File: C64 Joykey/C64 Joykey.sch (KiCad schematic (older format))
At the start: 25 parts, among them J1 Port_1, J2 Port_2, M1 Mounting, M2 Mounting, M3 Mounting, M4 Mounting, SW1 FIRE1, SW2 FIRE2, SW3 FIRE3, SW4 UP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

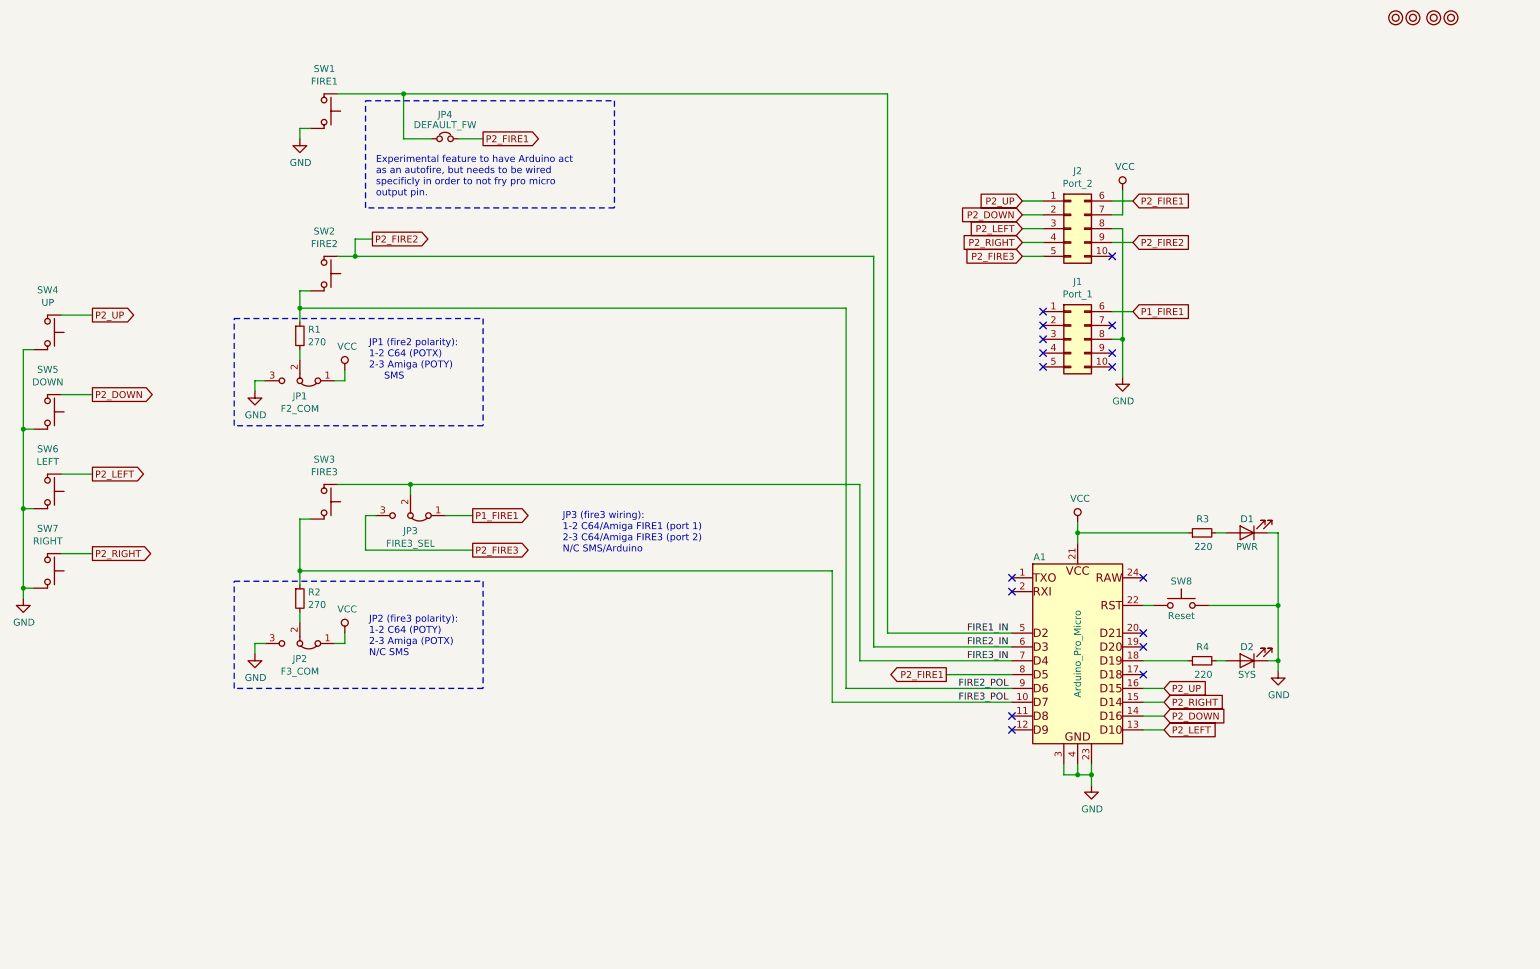
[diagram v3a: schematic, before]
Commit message: Tweaked PCB layout
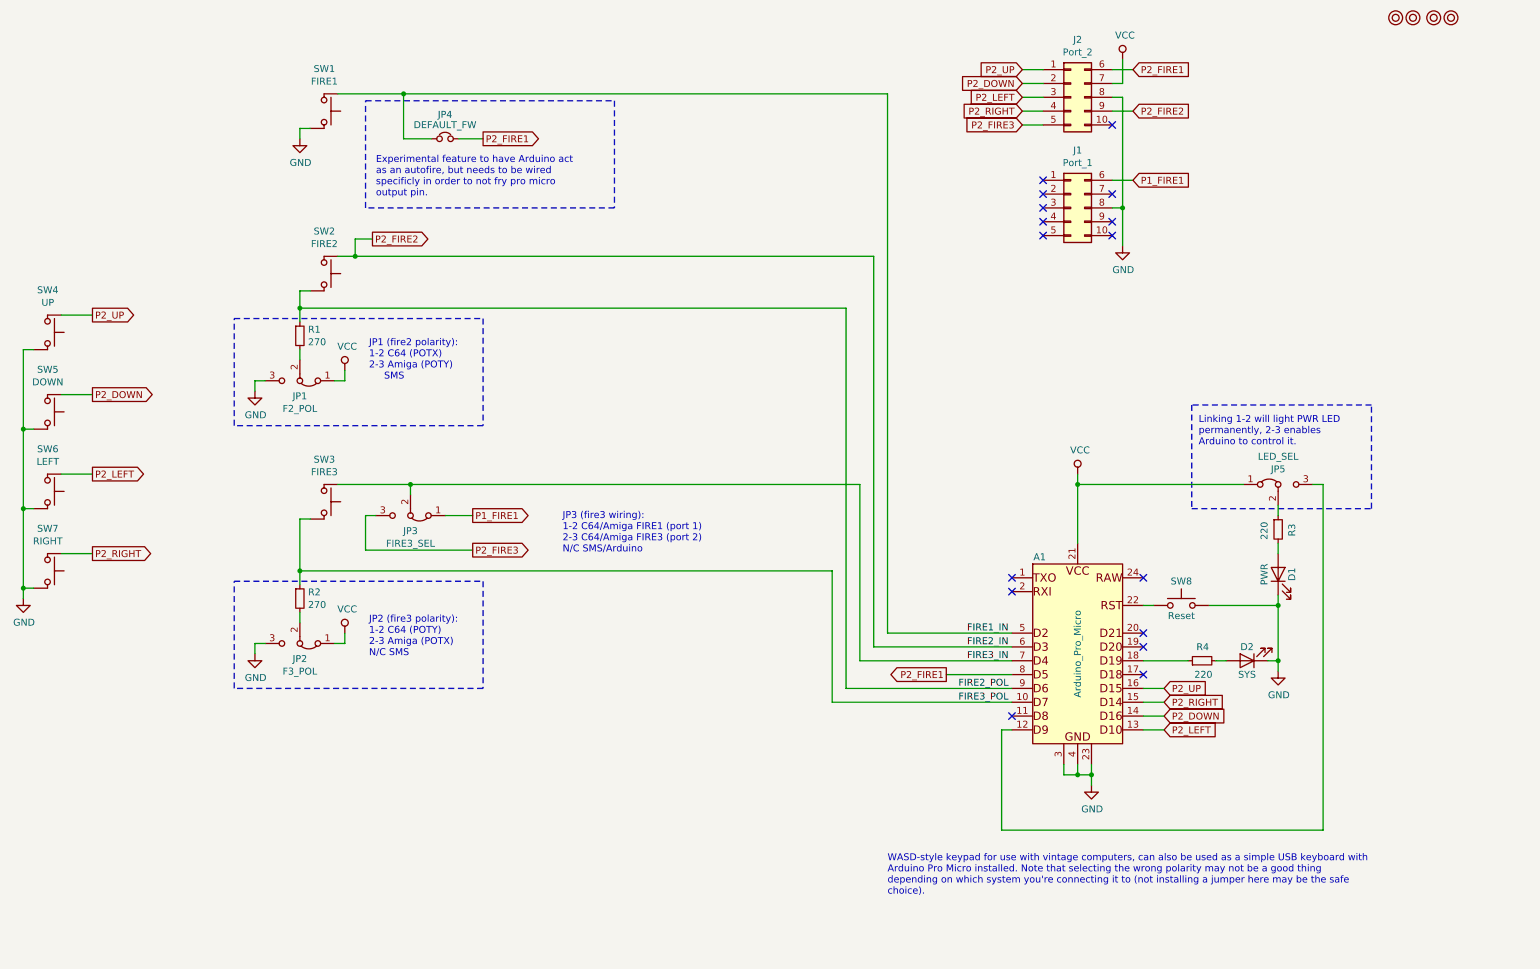
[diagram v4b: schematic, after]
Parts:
- added JP5: LED_SEL, solder_bridge:select, symbol Jumper:Jumper_3_Bridged12
- JP1: value F2_COM -> F2_POL
- JP2: value F3_COM -> F3_POL
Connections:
- net VCC: now also JP5.1 (A); no longer R3.1
- net at A1.12 (D9): now also JP5.3 (B)
- new net: JP5.2 (C), R3.1
- no-connect marks 17 -> 16
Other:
- note added: "Linking 1-2 will light PWR LED\npermanently, 2-3 enables\nArduino to control it."
- note added: "WASD-style keypad for use with vintage computers, can also be used as a simple USB keyboard with\nArduino Pro Micro installed. Note that selecting the wrong polarity may not be a good thing \ndepending on which system you're connecting it to (not installing a jumper here may be the safe\nchoice)."
- moved on the sheet: D1, J1, J2, R3
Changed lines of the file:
@@
 encoding utf-8
 Sheet 1 1
-Title "C64 Joykey"
+Title "C64 JoyKEY"
 Date ""
-Rev "A"
+Rev "B"
 Comp ""
 Comment1 ""
 Comment2 ""
-Comment3 "Note that due to the risk to shorting the wrong pin, it should be built hardwired."
-Comment4 "Joystick for C64/Amiga/SMS using directional keys."
+Comment3 ""
+Comment4 ""
 $EndDescr
 $Comp
@@
 L c64_idc:c64_idc J2
 U 1 1 5FB748C4
-P 8350 2075
-F 0 "J2" H 8400 2492 50  0000 C CNN
-F 1 "Port_2" H 8400 2401 50  0000 C CNN
-F 2 "C64 IDC:IDC_Joystick" H 8350 2075 50  0001 C CNN
-F 3 "~" H 8350 2075 50  0001 C CNN
-	1    8350 2075
+P 8350 1125
+F 0 "J2" H 8400 1542 50  0000 C CNN
+F 1 "Port_2" H 8400 1451 50  0000 C CNN
+F 2 "C64 IDC:IDC_Joystick" H 8350 1125 50  0001 C CNN
+F 3 "~" H 8350 1125 50  0001 C CNN
+	1    8350 1125
 	1    0    0    -1
 $EndComp
@@
 L Connector_Generic:Conn_02x05_Top_Bottom J1
 U 1 1 5FB76154
-P 8350 2875
-F 0 "J1" H 8400 3292 50  0000 C CNN
-F 1 "Port_1" H 8400 3201 50  0000 C CNN
-F 2 "C64 IDC:IDC_Joystick" H 8350 2875 50  0001 C CNN
-F 3 "~" H 8350 2875 50  0001 C CNN
-	1    8350 2875
+P 8350 1925
+F 0 "J1" H 8400 2342 50  0000 C CNN
+F 1 "Port_1" H 8400 2251 50  0000 C CNN
+F 2 "C64 IDC:IDC_Joystick" H 8350 1925 50  0001 C CNN
+F 3 "~" H 8350 1925 50  0001 C CNN
+	1    8350 1925
 	1    0    0    -1
 $EndComp
@@
 L power:GND #PWR03
 U 1 1 5FB76300
-P 8725 3150
-F 0 "#PWR03" H 8725 2900 50  0001 C CNN
-F 1 "GND" H 8730 2977 50  0000 C CNN
-F 2 "" H 8725 3150 50  0001 C CNN
-F 3 "" H 8725 3150 50  0001 C CNN
-	1    8725 3150
-	1    0    0    -1
-$EndComp
-NoConn ~ 8650 2275
-NoConn ~ 8650 3075
-Wire Wire Line
-	8650 1875 8800 1875
-Wire Wire Line
-	8650 2675 8800 2675
-Text GLabel 8800 1875 2    50   Input ~ 0
+P 8725 2200
+F 0 "#PWR03" H 8725 1950 50  0001 C CNN
+F 1 "GND" H 8730 2027 50  0000 C CNN
+F 2 "" H 8725 2200 50  0001 C CNN
+F 3 "" H 8725 2200 50  0001 C CNN
+	1    8725 2200
+	1    0    0    -1
+$EndComp
+NoConn ~ 8650 1325
+NoConn ~ 8650 2125
+Wire Wire Line
+	8650 925  8800 925
+Wire Wire Line
+	8650 1725 8800 1725
+Text GLabel 8800 925  2    50   Input ~ 0
 P2_FIRE1
-Text GLabel 8800 2675 2    50   Input ~ 0
+Text GLabel 8800 1725 2    50   Input ~ 0
 P1_FIRE1
 $Comp
 L power:VCC #PWR02
 U 1 1 5FB781A5
-P 8725 1800
-F 0 "#PWR02" H 8725 1650 50  0001 C CNN
-F 1 "VCC" H 8742 1973 50  0000 C CNN
-F 2 "" H 8725 1800 50  0001 C CNN
-F 3 "" H 8725 1800 50  0001 C CNN
-	1    8725 1800
-	1    0    0    -1
-$EndComp
-NoConn ~ 8150 2675
-NoConn ~ 8150 2775
-NoConn ~ 8150 2875
-NoConn ~ 8150 2975
-NoConn ~ 8150 3075
-NoConn ~ 8650 2775
-Text GLabel 8000 1875 0    50   Input ~ 0
+P 8725 850
+F 0 "#PWR02" H 8725 700 50  0001 C CNN
+F 1 "VCC" H 8742 1023 50  0000 C CNN
+F 2 "" H 8725 850 50  0001 C CNN
+F 3 "" H 8725 850 50  0001 C CNN
+	1    8725 850
+	1    0    0    -1
+$EndComp
+NoConn ~ 8150 1725
+NoConn ~ 8150 1825
+NoConn ~ 8150 1925
+NoConn ~ 8150 2025
+NoConn ~ 8150 2125
+NoConn ~ 8650 1825
+Text GLabel 8000 925  0    50   Input ~ 0
 P2_UP
 Wire Wire Line
-	8000 1875 8150 1875
-Text GLabel 8000 1975 0    50   Input ~ 0
+	8000 925  8150 925
+Text GLabel 8000 1025 0    50   Input ~ 0
 P2_DOWN
 Wire Wire Line
-	8150 1975 8000 1975
-Text GLabel 8000 2075 0    50   Input ~ 0
+	8150 1025 8000 1025
+Text GLabel 8000 1125 0    50   Input ~ 0
 P2_LEFT
 Wire Wire Line
-	8000 2075 8150 2075
-Text GLabel 8000 2175 0    50   Input ~ 0
+	8000 1125 8150 1125
+Text GLabel 8000 1225 0    50   Input ~ 0
 P2_RIGHT
 Wire Wire Line
-	8000 2175 8150 2175
-Text GLabel 8800 2175 2    50   Input ~ 0
+	8000 1225 8150 1225
+Text GLabel 8800 1225 2    50   Input ~ 0
 P2_FIRE2
 Wire Wire Line
-	8800 2175 8650 2175
+	8800 1225 8650 1225
 Text GLabel 4100 1425 2    50   Output ~ 0
 P2_FIRE1
-Text GLabel 8000 2275 0    50   Input ~ 0
+Text GLabel 8000 1325 0    50   Input ~ 0
 P2_FIRE3
 Wire Wire Line
-	8000 2275 8150 2275
+	8000 1325 8150 1325
 $Comp
 L sw_keyboard:SW_Keyboard SW4
@@
 P 2775 3175
 F 0 "JP1" H 2775 3286 50  0000 C CNN
-F 1 "F2_COM" H 2775 3377 50  0000 C CNN
+F 1 "F2_POL" H 2775 3377 50  0000 C CNN
 F 2 "Pin_Headers:Pin_Header_Angled_1x03_Pitch2.54mm" H 2775 3175 50  0001 C CNN
 F 3 "~" H 2775 3175 50  0001 C CNN
@@
 P 2775 5075
 F 0 "JP2" H 2775 5186 50  0000 C CNN
-F 1 "F3_COM" H 2775 5277 50  0000 C CNN
+F 1 "F3_POL" H 2775 5277 50  0000 C CNN
 F 2 "Pin_Headers:Pin_Header_Angled_1x03_Pitch2.54mm" H 2775 5075 50  0001 C CNN
 F 3 "~" H 2775 5075 50  0001 C CNN
@@
 	1050 4425 1275 4425
 $Comp
-L promicro:Arduino_Pro_Micro A1
-U 1 1 5FBBE539
-P 8400 4850
-F 0 "A1" H 8125 5250 50  0000 C CNN
-F 1 "Arduino_Pro_Micro" V 8400 4550 50  0000 C CNN
-F 2 "arduino_pro_micro:Arduino_Pro_Micro" H 8350 4850 50  0001 C CNN
-F 3 "~" H 8350 4850 50  0001 C CNN
-	1    8400 4850
-	1    0    0    -1
-$EndComp
-$Comp
 L Switch:SW_Push SW8
 U 1 1 5FBBF92E
@@
 L power:VCC #PWR0102
 U 1 1 5FBC8167
-P 8400 4200
-F 0 "#PWR0102" H 8400 4050 50  0001 C CNN
-F 1 "VCC" H 8417 4373 50  0000 C CNN
-F 2 "" H 8400 4200 50  0001 C CNN
-F 3 "" H 8400 4200 50  0001 C CNN
-	1    8400 4200
+P 8400 3850
+F 0 "#PWR0102" H 8400 3700 50  0001 C CNN
+F 1 "VCC" H 8417 4023 50  0000 C CNN
+F 2 "" H 8400 3850 50  0001 C CNN
+F 3 "" H 8400 3850 50  0001 C CNN
+	1    8400 3850
 	1    0    0    -1
 $EndComp
@@
 L Device:LED D1
 U 1 1 5FBD6E88
-P 9625 4275
-F 0 "D1" H 9625 4175 50  0000 C CNN
-F 1 "PWR" H 9625 4375 50  0000 C CNN
-F 2 "LEDs:LED_D5.0mm" H 9625 4275 50  0001 C CNN
-F 3 "~" H 9625 4275 50  0001 C CNN
-	1    9625 4275
-	-1   0    0    1
-$EndComp
-Wire Wire Line
-	9775 4275 9850 4275
+P 9850 4575
+F 0 "D1" H 9850 4475 50  0000 C CNN
+F 1 "PWR" H 9850 4675 50  0000 C CNN
+F 2 "LEDs:LED_D5.0mm" H 9850 4575 50  0001 C CNN
+F 3 "~" H 9850 4575 50  0001 C CNN
+	1    9850 4575
+	0    -1   -1   0
+$EndComp
 $Comp
 L Device:R_Small R3
 U 1 1 5FBD9406
-P 9300 4275
-F 0 "R3" V 9400 4225 50  0000 L CNN
-F 1 "220" V 9200 4200 50  0000 L CNN
-F 2 "Resistors_THT:R_Axial_DIN0207_L6.3mm_D2.5mm_P7.62mm_Horizontal" H 9300 4275 50  0001 C CNN
-F 3 "~" H 9300 4275 50  0001 C CNN
-	1    9300 4275
-	0    -1   -1   0
-$EndComp
-Wire Wire Line
-	8400 4275 8400 4200
-Wire Wire Line
-	8400 4275 8400 4350
-Connection ~ 8400 4275
+P 9850 4250
+F 0 "R3" V 9950 4200 50  0000 L CNN
+F 1 "220" V 9750 4175 50  0000 L CNN
+F 2 "Resistors_THT:R_Axial_DIN0207_L6.3mm_D2.5mm_P7.62mm_Horizontal" H 9850 4250 50  0001 C CNN
+F 3 "~" H 9850 4250 50  0001 C CNN
+	1    9850 4250
+	1    0    0    -1
+$EndComp
+Wire Wire Line
+	8400 3925 8400 3850
+Connection ~ 8400 3925
 $Comp
 L Device:LED D2
@@
 Connection ~ 9850 5200
 Wire Wire Line
-	9850 4800 9850 4275
-Connection ~ 9850 4800
-Wire Wire Line
-	9400 4275 9475 4275
-Wire Wire Line
-	8400 4275 9200 4275
+	9850 4350 9850 4425
 Wire Wire Line
 	8875 4800 8950 4800
@@
 NoConn ~ 8875 5300
 Wire Wire Line
-	8650 2875 8725 2875
-Connection ~ 8725 2875
-Wire Wire Line
-	8725 2875 8725 3150
-NoConn ~ 8650 2975
-Wire Wire Line
-	8650 2075 8725 2075
-Wire Wire Line
-	8725 2075 8725 2875
-Wire Wire Line
-	8650 1975 8725 1975
-Wire Wire Line
-	8725 1975 8725 1800
+	8650 1925 8725 1925
+Connection ~ 8725 1925
+Wire Wire Line
+	8725 1925 8725 2200
+NoConn ~ 8650 2025
+Wire Wire Line
+	8650 1125 8725 1125
+Wire Wire Line
+	8725 1125 8725 1925
+Wire Wire Line
+	8650 1025 8725 1025
+Wire Wire Line
+	8725 1025 8725 850
 Text GLabel 9025 5500 2    50   Input ~ 0
 P2_RIGHT
@@
 Text Notes 4675 4425 0    50   ~ 0
 JP3 (fire3 wiring):\n1-2 C64/Amiga FIRE1 (port 1)\n2-3 C64/Amiga FIRE3 (port 2)\nN/C SMS/Arduino
-NoConn ~ 7925 5700
-NoConn ~ 7925 5600
 Wire Wire Line
 	3575 3925 6825 3925
@@
 Wire Wire Line
 	3525 1100 3525 1425
+$Comp
+L promicro:Arduino_Pro_Micro A1
+U 1 1 5FBBE539
+P 8400 4850
+F 0 "A1" H 8125 5250 50  0000 C CNN
+F 1 "Arduino_Pro_Micro" V 8400 4550 50  0000 C CNN
+F 2 "arduino_pro_micro:Arduino_Pro_Micro" H 8350 4850 50  0001 C CNN
+F 3 "~" H 8350 4850 50  0001 C CNN
+	1    8400 4850
+	1    0    0    -1
+$EndComp
+$Comp
+L Jumper:Jumper_3_Bridged12 JP5
+U 1 1 60BF4B55
+P 9850 3925
+F 0 "JP5" H 9850 4036 50  0000 C CNN
+F 1 "LED_SEL" H 9850 4127 50  0000 C CNN
+F 2 "solder_bridge:select" H 9850 3925 50  0001 C CNN
+F 3 "~" H 9850 3925 50  0001 C CNN
+	1    9850 3925
+	1    0    0    -1
+$EndComp
+Wire Wire Line
+	9850 4725 9850 4800
+Connection ~ 9850 4800
+Wire Wire Line
+	8400 3925 8400 4350
+Wire Wire Line
+	8400 3925 9600 3925
+Wire Wire Line
+	7925 5700 7850 5700
+Wire Wire Line
+	7850 5700 7850 6425
+Wire Wire Line
+	7850 6425 10175 6425
+Wire Wire Line
+	10175 6425 10175 3925
+Wire Wire Line
+	10175 3925 10100 3925
+Wire Wire Line
+	9850 4075 9850 4150
+NoConn ~ 7925 5600
+Text Notes 9275 3650 0    50   ~ 0
+Linking 1-2 will light PWR LED\npermanently, 2-3 enables\nArduino to control it.
+Wire Notes Line
+	10525 4100 10525 3350
+Wire Notes Line
+	10525 3350 9225 3350
+Wire Notes Line
+	9225 3350 9225 4100
+Wire Notes Line
+	9225 4100 10525 4100
+Text Notes 7025 6900 0    50   ~ 0
+WASD-style keypad for use with vintage computers, can also be used as a simple USB keyboard with\nArduino Pro Micro installed. Note that selecting the wrong polarity may not be a good thing \ndepending on which system you're connecting it to (not installing a jumper here may be the safe\nchoice).
 $EndSCHEMATC
